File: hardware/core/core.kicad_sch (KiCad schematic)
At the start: 32 parts, among them J17 PROG, J18 USB_C_Receptacle_USB2.0_14P, J5 TO_NEXT, J7 TO_NEXT, J8 Conn_02x09_Odd_Even, SW1 RESET, SW2 BOOT, U10 SN74AHCT1G14DCKR, U19 ESP32-S3-MINI-1, U20 AP2112K-3.3TRG1, U21 SN65HVD230DR

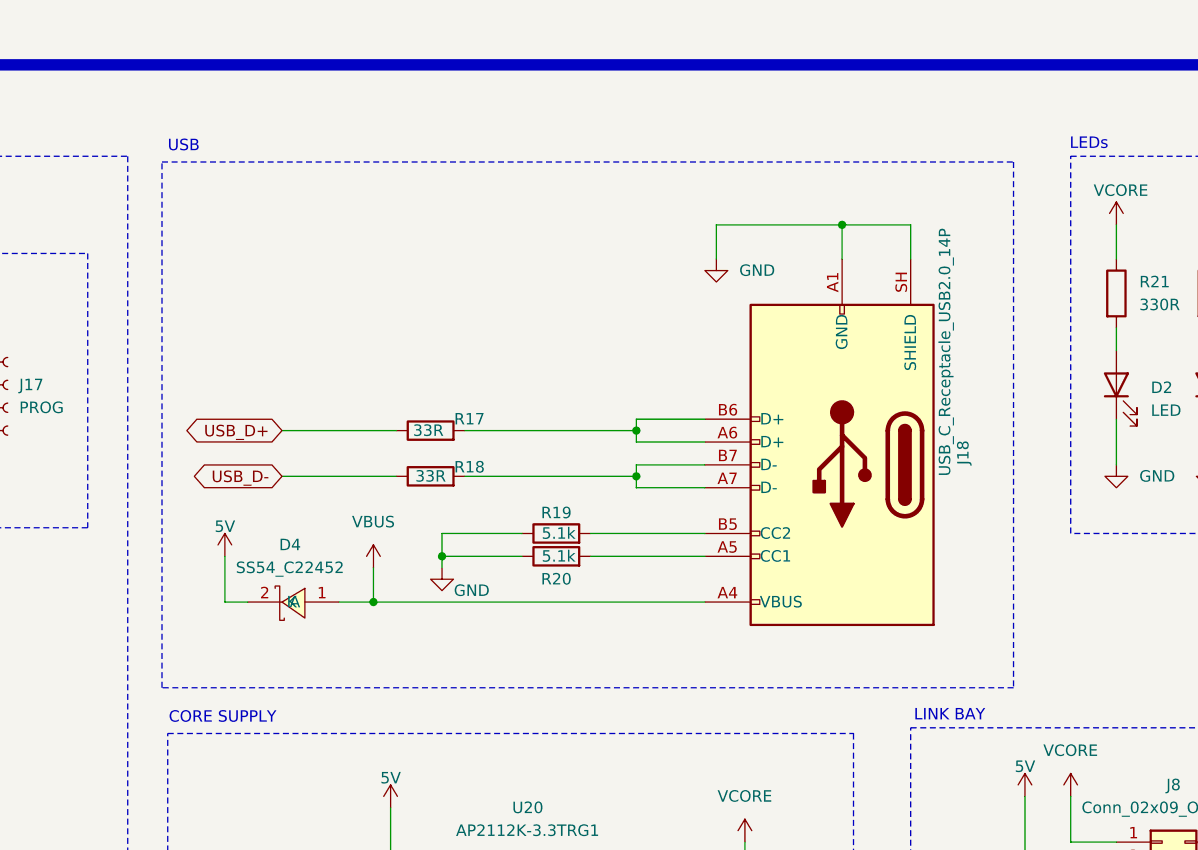
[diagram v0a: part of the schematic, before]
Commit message: fix(hardware): finalize core layout and USB constraints
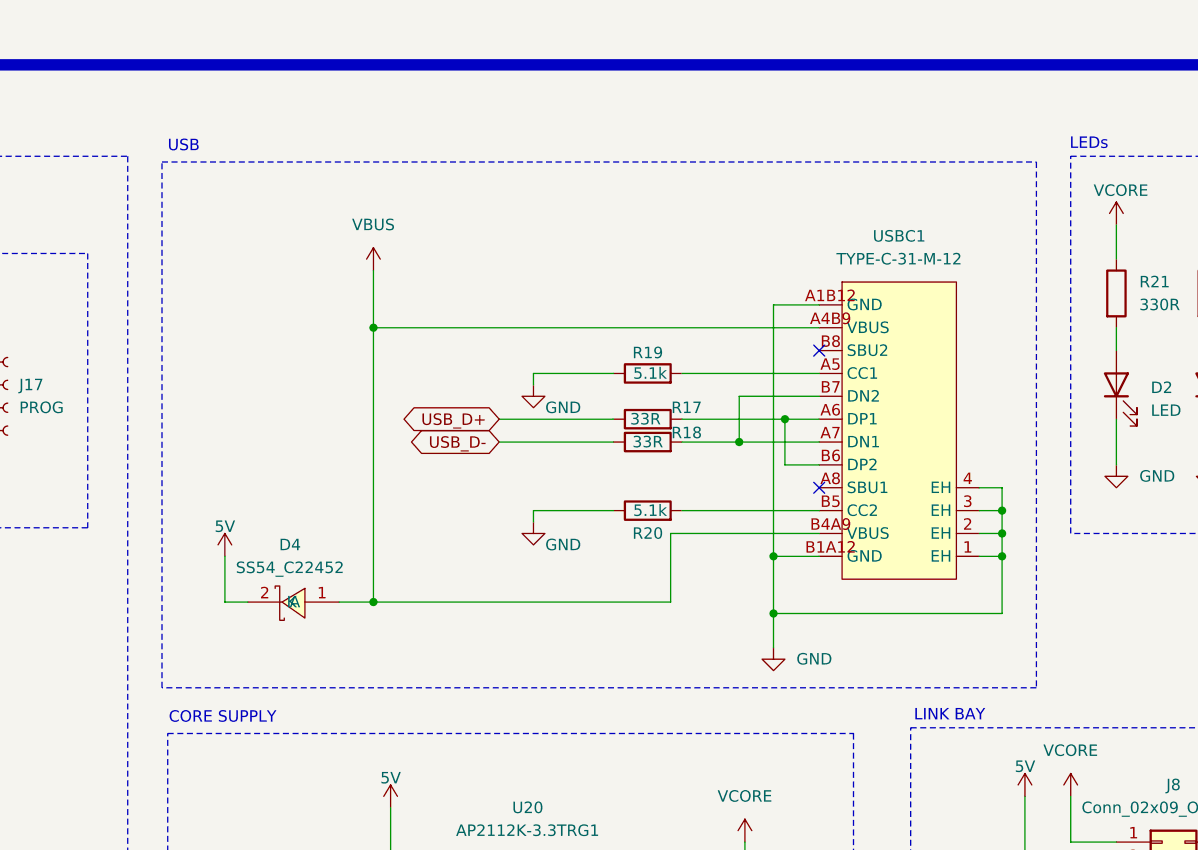
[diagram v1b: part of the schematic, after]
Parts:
- removed J18: USB_C_Receptacle_USB2.0_14P, SpaghettiLAB2:USB-C-SMD_TYPEC-324G-BCP24, symbol Connector:USB_C_Receptacle_USB2.0_14P
- added USBC1: TYPE-C-31-M-12, SpaghettiLAB:USB-C_SMD-TYPE-C-31-M-12_1, symbol SpaghettiLAB:TYPE-C-31-M-12
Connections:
- net GND: now also USBC1.1 (EH), USBC1.2 (EH), USBC1.3 (EH), USBC1.4 (EH), USBC1.A1B12 (GND), USBC1.B1A12 (GND); no longer SW1.3
- net VBUS: now also USBC1.A4B9 (VBUS), USBC1.B4A9 (VBUS)
- net at R15.2, U19.4 (IO0): now also SW2.3; no longer SW2.2
- net at C73.1, R16.2, U19.45 (EN): now also SW1.3; no longer SW1.2
- net at R20.2: now also USBC1.B5 (CC2)
- net at R17.2: now also USBC1.A6 (DP1), USBC1.B6 (DP2)
- net at R18.2: now also USBC1.A7 (DN1), USBC1.B7 (DN2)
- net at R19.2: now also USBC1.A5 (CC1)
- no-connect marks 9 -> 11
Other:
- moved on the sheet: R17, R18, R20

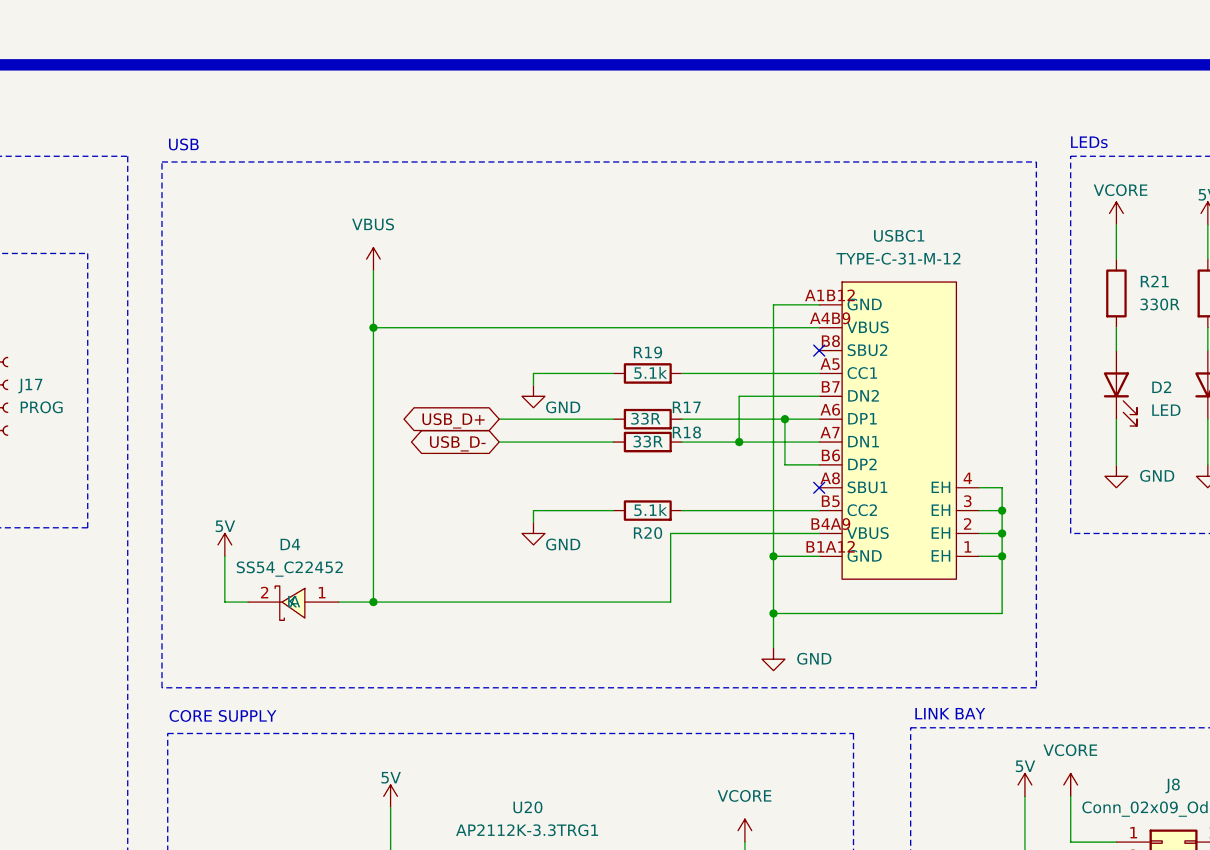
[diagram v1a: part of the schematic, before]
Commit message: feat(hardware): update core USB-C connector
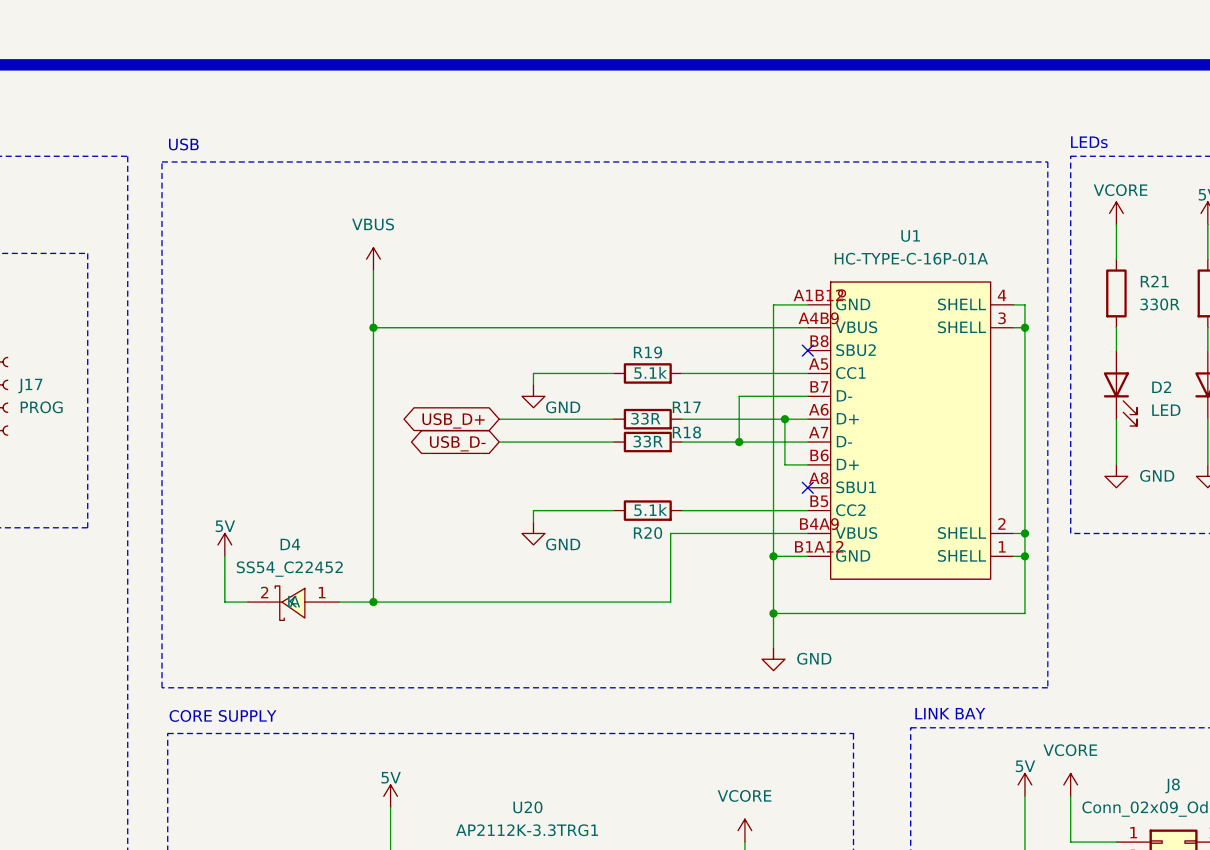
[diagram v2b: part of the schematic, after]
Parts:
- removed USBC1: TYPE-C-31-M-12, SpaghettiLAB:USB-C_SMD-TYPE-C-31-M-12_1, symbol SpaghettiLAB:TYPE-C-31-M-12
- added U1: HC-TYPE-C-16P-01A, SpaghettiLAB:USB-C-SMD_HC-TYPE-C-16P-01A, symbol SpaghettiLAB:HC-TYPE-C-16P-01A
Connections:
- net GND: now also U1.1 (SHELL), U1.2 (SHELL), U1.3 (SHELL), U1.4 (SHELL), U1.A1B12 (GND), U1.B1A12 (GND)
- net VBUS: now also U1.A4B9 (VBUS), U1.B4A9 (VBUS)
- net at R19.2: now also U1.A5 (CC1)
- net at R17.2: now also U1.A6 (D+), U1.B6 (D+)
- net at R18.2: now also U1.A7 (D-), U1.B7 (D-)
- net at R20.2: now also U1.B5 (CC2)

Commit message: Fixed silkscreen text
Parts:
- removed R19: 5.1k, SpaghettiLAB2:R0603, symbol Device:R
- added J1: ARGB, Connector_PinHeader_2.54mm:PinHeader_1x03_P2.54mm_Vertical, symbol Connector:Conn_01x03_Pin
- added R23: 5.1k, SpaghettiLAB:R0603, symbol Device:R
- C14, C24, C73, C74, C75, C76, C77, C78: footprint SpaghettiLAB2:C0603 -> SpaghettiLAB:C0603
- D2, D3: footprint SpaghettiLAB2:LED0603-RD -> SpaghettiLAB:LED0603-RD
- LED2: footprint SpaghettiLAB2:LED-SMD_4P-L3.2-W2.8-LS5.9_SK6812MINI-E -> SpaghettiLAB:LED-SMD_4P-L3.2-W2.8-LS5.9_SK6812MINI-E
- R10, R15, R16, R17, R18, R20, R21, R22: footprint SpaghettiLAB2:R0603 -> SpaghettiLAB:R0603
- SW1, SW2: footprint SpaghettiLAB2:SW-SMD_4P-L5.1-W5.1-P3.70-LS6.5-TL_H1.5 -> SpaghettiLAB:SW-SMD_4P-L5.1-W5.1-P3.70-LS6.5-TL_H1.5
- U10: footprint SpaghettiLAB2:SOT-353_L2.2-W1.4-P0.65-LS2.4-BR -> SpaghettiLAB:SOT-353_L2.2-W1.4-P0.65-LS2.4-BR
- U20: footprint SpaghettiLAB2:SOT-25-5_L2.9-W1.6-P0.95-LS2.8-BL -> SpaghettiLAB:SOT-25-5_L2.9-W1.6-P0.95-LS2.8-BL
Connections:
- net 5V: now also J1.1 (Pin_1)
- net GND: now also J1.3 (Pin_3), R23.1
- net PROG_TX: now reaches J17.3 (Pin_3), U19.39 (TXD0)
- net PROG_RX: now reaches J17.2 (Pin_2), U19.40 (RXD0)
- net CC1: now reaches U1.A5 (CC1)
- net CC1: now also R23.2
- net CC2: now reaches R20.2, U1.B5 (CC2)
- net DOUT: now reaches LED2.4 (DOUT)
- net DOUT: now also J1.2 (Pin_2)
- no-connect marks 11 -> 10

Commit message: removed rgb led from core
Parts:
- removed C24: 100nF, SpaghettiLAB:C0603, symbol STMICRO:root_1_GRM033C71A104KE14D_STMICRO.SchLib
- removed LED2: SK6812MINI-E, SpaghettiLAB:LED-SMD_4P-L3.2-W2.8-LS5.9_SK6812MINI-E, symbol USBC_PD_mo-easyedapro:SK6812MINI-E_C5149201
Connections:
- net DOUT: now also U10.4 (Y)
